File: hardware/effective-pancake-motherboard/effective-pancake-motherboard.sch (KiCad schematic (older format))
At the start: 45 parts, among them J1 Conn_02x05_Odd_Even, J2 Conn_02x04_Odd_Even, J5 QTR-1A_Conn, J6 QTR-1A_Conn, U1 Teensy_3.2, U3 Teensy_3.6, U4 SN74AHCT125N, U5 TMC2660-BOB, U6 TMC2660-BOB, U7 TMC2660-BOB

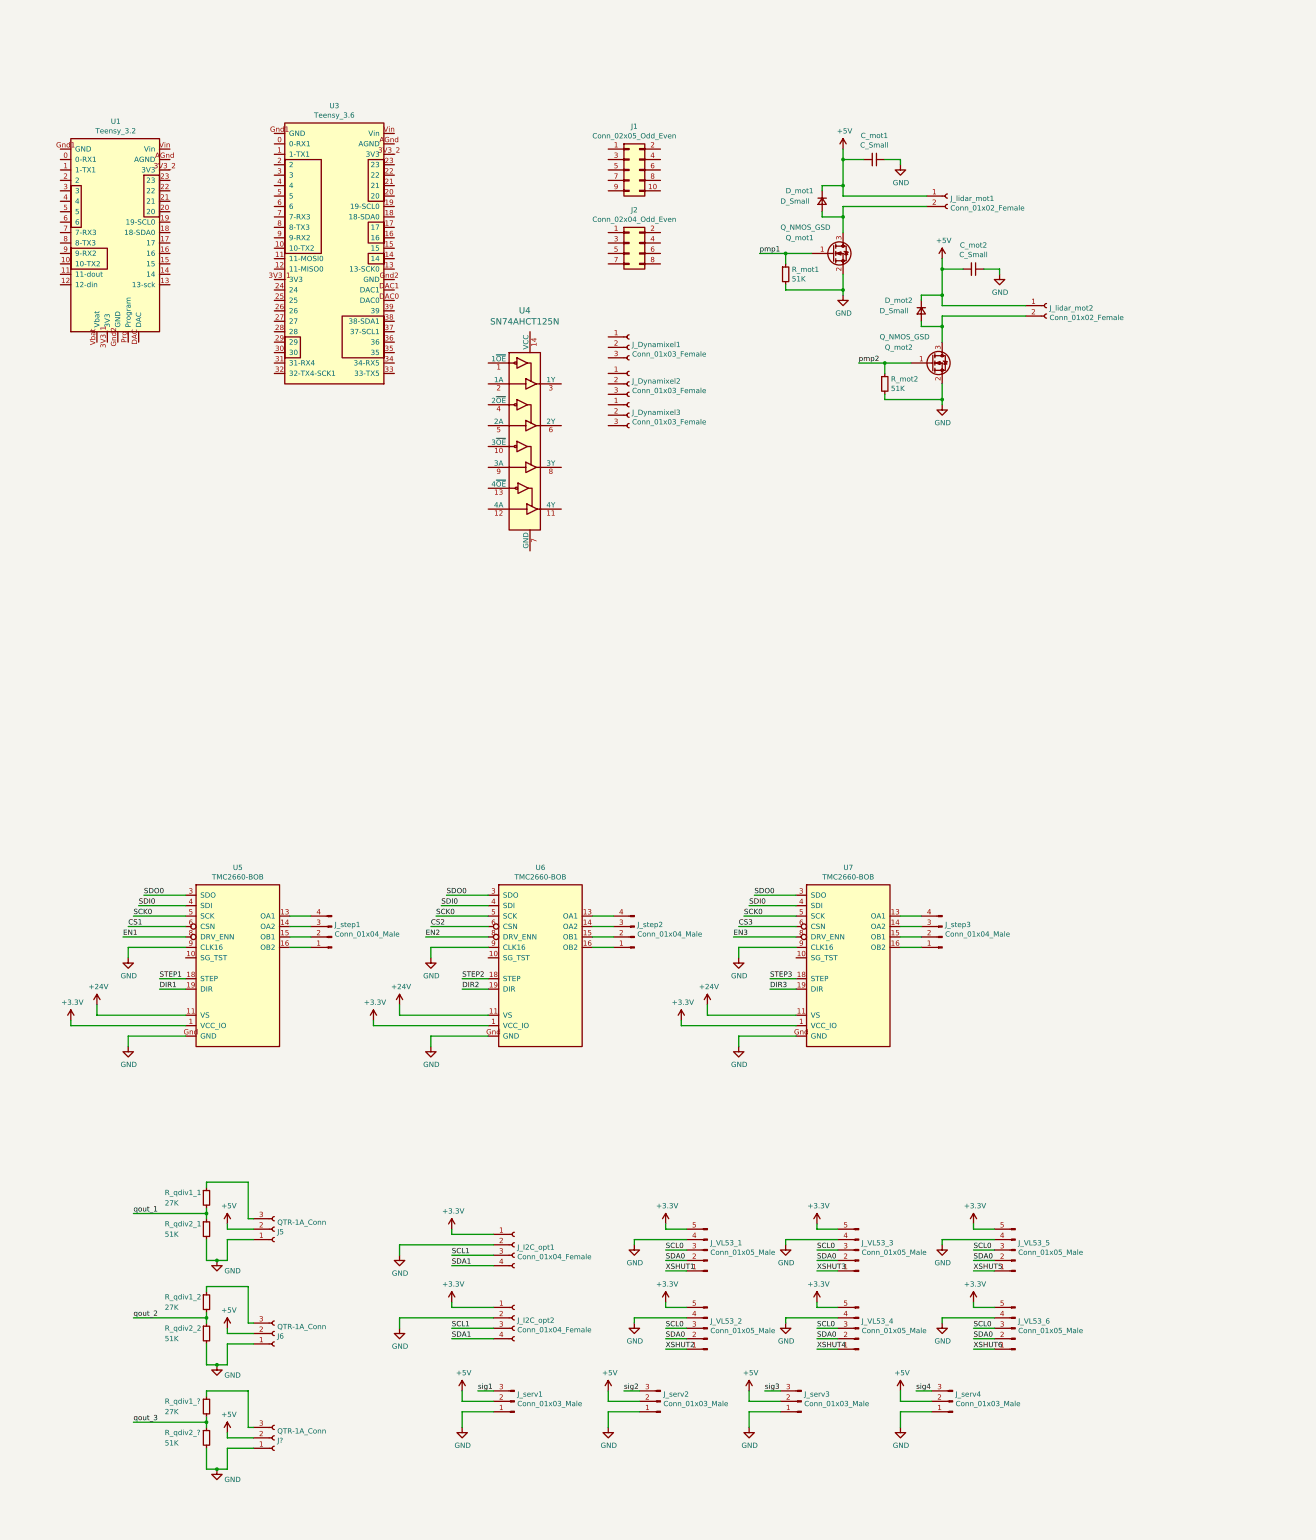
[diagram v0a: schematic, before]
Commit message: Finished schematics, fp association, and verifications.
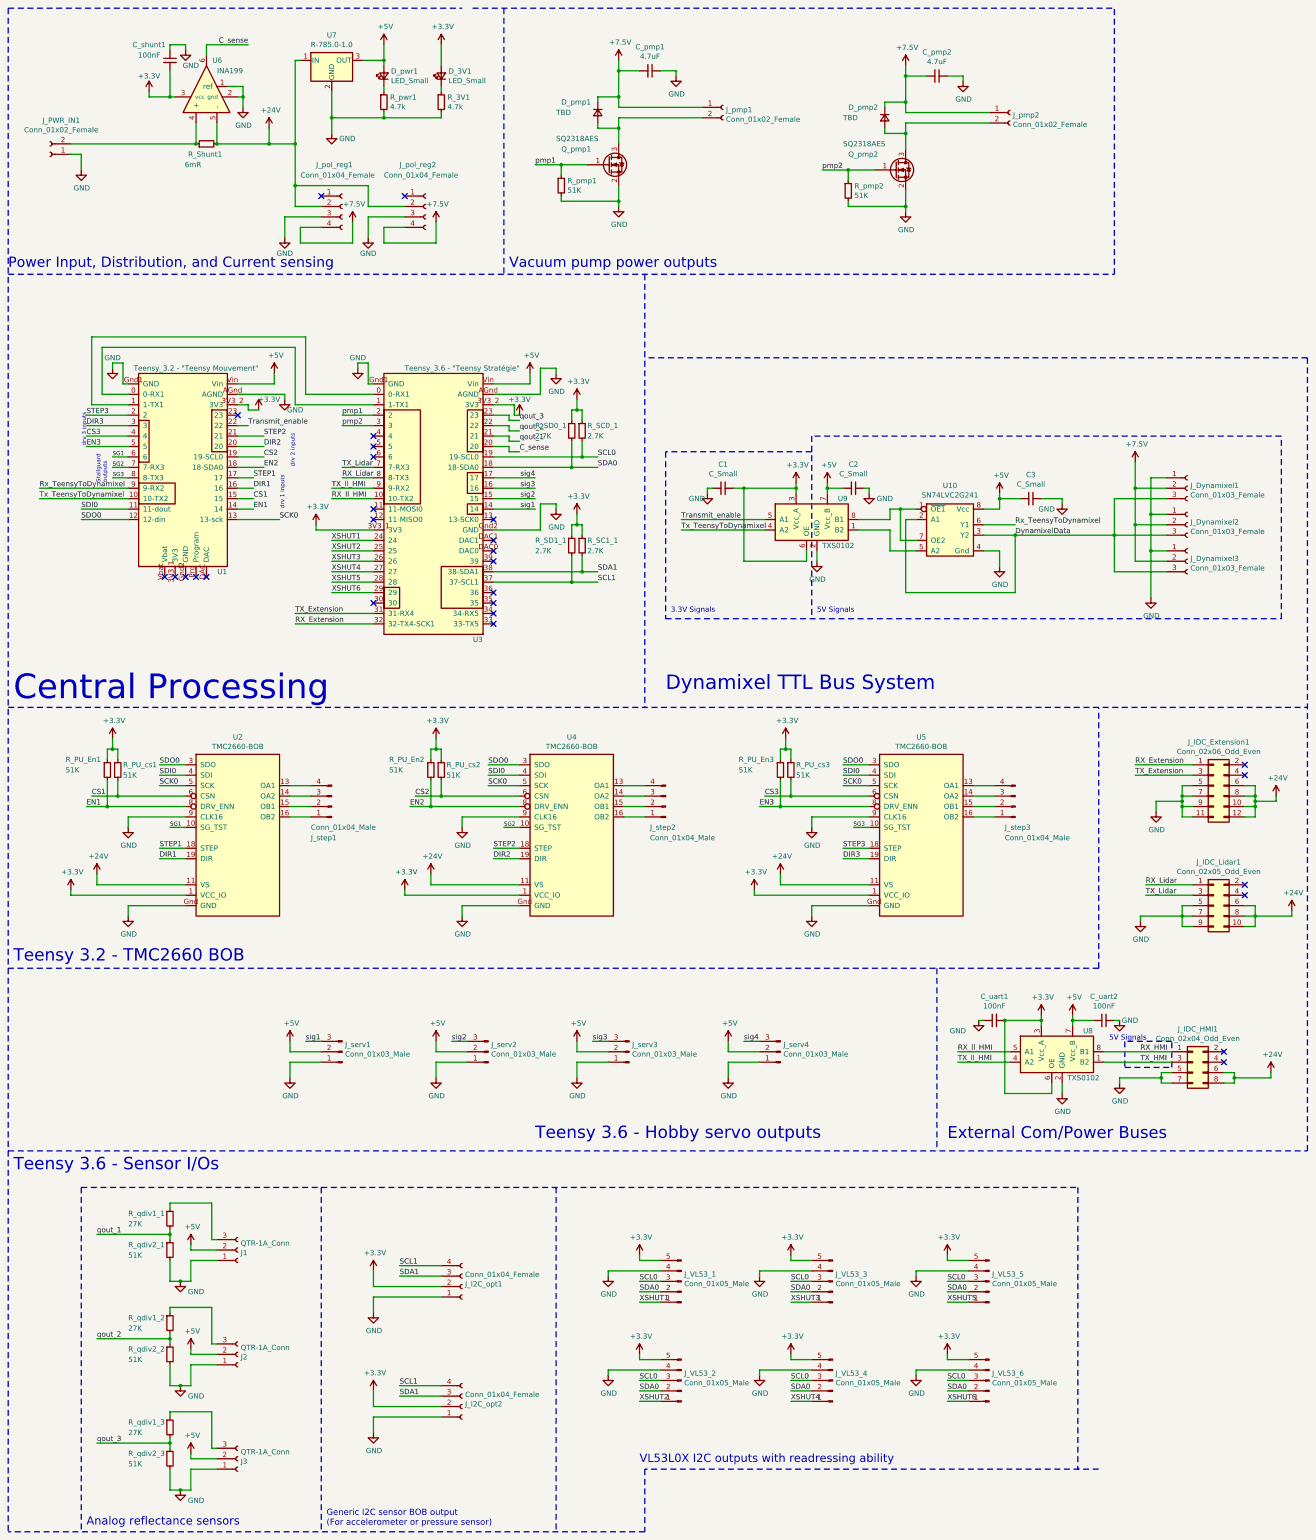
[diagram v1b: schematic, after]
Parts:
- removed U4: SN74AHCT125N, digikey-footprints:DIP-14_W3mm, symbol dk_Logic-Buffers-Drivers-Receivers-Transceivers:SN74AHCT125N
- added C1, C2, C3: C_Small, Capacitor_SMD:C_0805_2012Metric_Pad1.15x1.40mm_HandSolder, symbol Device:C_Small
- added C_shunt1, C_uart1, C_uart2: 100nF, Capacitor_SMD:C_0805_2012Metric_Pad1.15x1.40mm_HandSolder, symbol Device:C_Small
- added D_3V1, D_pwr1: LED_Small, LED_SMD:LED_1206_3216Metric_Castellated, symbol Device:LED_Small
- added J_IDC_Extension1: Conn_02x06_Odd_Even, Connector_IDC:IDC-Header_2x06_P2.54mm_Vertical, symbol Connector_Generic:Conn_02x06_Odd_Even
- added J_PWR_IN1: Conn_01x02_Female, Connector_Phoenix_MC_HighVoltage:PhoenixContact_MC_1,5_2-G-5.08_1x02_P5.08mm_Horizontal, symbol Connector:Conn_01x02_Female
- added J_pol_reg1, J_pol_reg2: Conn_01x04_Female, Connector_PinSocket_2.54mm:PinSocket_1x04_P2.54mm_Vertical, symbol Connector:Conn_01x04_Female
- added R_3V1, R_pwr1: 4.7k, Resistor_SMD:R_0805_2012Metric_Pad1.15x1.40mm_HandSolder, symbol Device:R_Small
- added R_PU_En1, R_PU_En2, R_PU_En3, R_PU_cs1, R_PU_cs2, R_PU_cs3: 51K, Resistor_SMD:R_0805_2012Metric_Pad1.15x1.40mm_HandSolder, symbol Device:R_Small
- added R_SC0_1, R_SC1_1, R_SD0_1, R_SD1_1: 2.7K, Resistor_SMD:R_0805_2012Metric_Pad1.15x1.40mm_HandSolder, symbol Device:R_Small
- added R_Shunt1: 6mR, Resistor_SMD:R_1206_3216Metric_Pad1.42x1.75mm_HandSolder, symbol Device:R_Small
- added U10: SN74LVC2G241, effective-pancake_fp:PDSO-G8, symbol effective-pancake-global:SN74LVC2G241
- added U6: INA199, Package_TO_SOT_SMD:Texas_R-PDSO-G6, symbol effective-pancake-global:INA199
- added U7: R-785.0-1.0, Converter_DCDC:Converter_DCDC_RECOM_R-78E-0.5_THT, symbol effective-pancake-global:R-785.0-1.0
- added U8, U9: TXS0102, effective-pancake_fp:PDSO-G8, symbol effective-pancake-global:TXS0102
- C_pmp1: renamed from C_mot1; value C_Small -> 4.7uF; footprint (none) -> Capacitor_THT:C_Radial_D4.0mm_H7.0mm_P1.50mm
- C_pmp2: renamed from C_mot2; value C_Small -> 4.7uF; footprint (none) -> Capacitor_THT:C_Radial_D4.0mm_H7.0mm_P1.50mm
- D_pmp1: renamed from D_mot1; value D_Small -> TBD; footprint (none) -> Diode_SMD:D_1206_3216Metric
- D_pmp2: renamed from D_mot2; value D_Small -> TBD; footprint (none) -> Diode_SMD:D_1206_3216Metric
- J_Dynamixel1, J_Dynamixel2, J_Dynamixel3: footprint (none) -> Connector_Molex:Molex_Micro-Latch_53253-0370_1x03_P2.00mm_Vertical
- J_I2C_opt1, J_I2C_opt2: footprint (none) -> Connector_PinSocket_2.54mm:PinSocket_1x04_P2.54mm_Vertical
- J_IDC_HMI1: renamed from J2; footprint (none) -> Connector_IDC:IDC-Header_2x04_P2.54mm_Vertical
- J_IDC_Lidar1: renamed from J1; footprint (none) -> Connector_IDC:IDC-Header_2x05_P2.54mm_Vertical
- J_VL53_1, J_VL53_2, J_VL53_3, J_VL53_4, J_VL53_5, J_VL53_6: footprint (none) -> Connector_PinSocket_2.54mm:PinSocket_1x05_P2.54mm_Vertical
- J_pmp1: renamed from J_lidar_mot1; footprint (none) -> Connector_JST:JST_XH_B2B-XH-A_1x02_P2.50mm_Vertical
- J_pmp2: renamed from J_lidar_mot2; footprint (none) -> Connector_JST:JST_XH_B2B-XH-A_1x02_P2.50mm_Vertical
- J_serv1, J_serv2, J_serv3, J_serv4: footprint (none) -> Connector_PinHeader_2.54mm:PinHeader_1x03_P2.54mm_Vertical
- J_step1, J_step2, J_step3: footprint (none) -> Connector_PinHeader_2.54mm:PinHeader_1x04_P2.54mm_Vertical
- Q_pmp1: renamed from Q_mot1; value Q_NMOS_GSD -> SQ2318AES; footprint (none) -> Package_TO_SOT_SMD:SOT-23
- Q_pmp2: renamed from Q_mot2; value Q_NMOS_GSD -> SQ2318AES; footprint (none) -> Package_TO_SOT_SMD:SOT-23
- R_pmp1: renamed from R_mot1; footprint (none) -> Resistor_SMD:R_0805_2012Metric_Pad1.15x1.40mm_HandSolder
- R_pmp2: renamed from R_mot2; footprint (none) -> Resistor_SMD:R_0805_2012Metric_Pad1.15x1.40mm_HandSolder
- U1: value Teensy_3.2 -> Teensy_3.2 - \"Teensy Mouvement\"; footprint (none) -> digikey-footprints:Teensy_3.2
- U2: renamed from U5; footprint (none) -> effective-pancake_fp:TMC2660-BOB
- U3: value Teensy_3.6 -> Teensy_3.6 - \"Teensy Stratégie\"; footprint (none) -> effective-pancake_fp:Teensy_3.6
- U4: renamed from U6; footprint (none) -> effective-pancake_fp:TMC2660-BOB
- U5: renamed from U7; footprint (none) -> effective-pancake_fp:TMC2660-BOB
- gave numbers to parts that had none: 3
- renumbered J5 to J1, J6 to J2
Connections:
- net +24V: now also J_IDC_HMI1.6 (Pin_6), J_IDC_HMI1.8 (Pin_8), J_IDC_Lidar1.10 (Pin_10), J_IDC_Lidar1.6 (Pin_6), J_IDC_Lidar1.8 (Pin_8), J_IDC_Extension1.10 (Pin_10), J_IDC_Extension1.12 (Pin_12), J_IDC_Extension1.6 (Pin_6), J_IDC_Extension1.8 (Pin_8), J_pol_reg1.2 (Pin_2), J_pol_reg2.2 (Pin_2), R_Shunt1.2, U6.5 (-), U7.1 (IN)
- net +3V3: now also J_I2C_opt1.2 (Pin_2), J_I2C_opt2.2 (Pin_2), U1.3V3_2 (3V3), U3.3V3_1 (3V3), U3.3V3_2 (3V3), C1.1, C_shunt1.2, C_uart1.2, D_3V1.2 (A), R_PU_En1.1, R_PU_En2.1, R_PU_En3.1, R_PU_cs1.1, R_PU_cs2.1, R_PU_cs3.1, R_SC0_1.1, R_SC1_1.1, R_SD0_1.1, R_SD1_1.1, U6.3 (vcc), U8.3 (Vcc_A), U8.6 (OE), U9.3 (Vcc_A), U9.6 (OE); no longer J_I2C_opt1.1 (Pin_1), J_I2C_opt2.1 (Pin_1)
- net +5V: now also U1.Vin, U3.Vin, C2.2, C3.2, C_uart2.2, D_pwr1.2 (A), U10.8 (Vcc), U7.3 (OUT), U8.7 (Vcc_B), U9.7 (Vcc_B); no longer C_pmp1.2, C_pmp2.2, D_pmp1.1 (K), D_pmp2.1 (K), J_pmp1.1 (Pin_1), J_pmp2.1 (Pin_1)
- net CS1: now also U1.15, R_PU_cs1.2
- net CS2: now also U1.19 (19-SCL0), R_PU_cs2.2
- net CS3: now also U1.4, R_PU_cs3.2
- net DIR1: now also U1.16
- net DIR2: now also U1.20
- net DIR3: now also U1.3
- net EN1: now also U1.14, R_PU_En1.2
- net EN2: now also U1.18 (18-SDA0), R_PU_En2.2
- net EN3: now also U1.5, R_PU_En3.2
- net GND: now also J_Dynamixel1.1 (Pin_1), J_Dynamixel2.1 (Pin_1), J_Dynamixel3.1 (Pin_1), J_I2C_opt1.1 (Pin_1), J_I2C_opt2.1 (Pin_1), J_IDC_HMI1.5 (Pin_5), J_IDC_HMI1.7 (Pin_7), J_IDC_Lidar1.5 (Pin_5), J_IDC_Lidar1.7 (Pin_7), J_IDC_Lidar1.9 (Pin_9), U1.AGnd (AGND), U1.Gnd1 (GND), U3.AGnd (AGND), U3.Gnd1 (GND), U3.Gnd2 (GND), C1.2, C2.1, C3.1, C_shunt1.1, C_uart1.1, C_uart2.1, J_IDC_Extension1.11 (Pin_11), J_IDC_Extension1.5 (Pin_5), J_IDC_Extension1.7 (Pin_7), J_IDC_Extension1.9 (Pin_9), J_PWR_IN1.1 (Pin_1), J_pol_reg1.3 (Pin_3), J_pol_reg2.3 (Pin_3), R_3V1.2, R_pwr1.2, U10.4 (Gnd), U6.1 (ref), U6.2 (gnd), U7.2 (GND), U8.2 (GND), U9.2 (GND); no longer J_I2C_opt1.2 (Pin_2), J_I2C_opt2.2 (Pin_2)
- net SCK0: now also U1.13 (13-sck)
- net SCL0: now also U3.19 (19-SCL0), R_SC0_1.2
- net SCL1: now also J_I2C_opt1.4 (Pin_4), J_I2C_opt2.4 (Pin_4), U3.37 (37-SCL1), R_SD1_1.2; no longer J_I2C_opt1.3 (Pin_3), J_I2C_opt2.3 (Pin_3)
- net SDA0: now also U3.18 (18-SDA0), R_SD0_1.2
- net SDA1: now also J_I2C_opt1.3 (Pin_3), J_I2C_opt2.3 (Pin_3), U3.38 (38-SDA1), R_SC1_1.2; no longer J_I2C_opt1.4 (Pin_4), J_I2C_opt2.4 (Pin_4)
- net SDI0: now also U1.11 (11-dout)
- net SDO0: now also U1.12 (12-din)
- net STEP1: now also U1.17
- net STEP2: now also U1.21
- net STEP3: now also U1.2
- net XSHUT1: now also U3.24
- net XSHUT2: now also U3.25
- net XSHUT3: now also U3.26
- net XSHUT4: now also U3.27
- net XSHUT5: now also U3.28
- net XSHUT6: now also U3.29
- net pmp1: now also U3.2
- net pmp2: now also U3.3
- net qout_1: now also U3.21
- net qout_2: now also U3.22
- net qout_3: now also U3.23
- net sig1: now also U3.14
- net sig2: now also U3.15
- net sig3: now also U3.16
- net sig4: now also U3.17
- net at U1.0 (0-RX1): now also U3.1 (1-TX1)
- net at U1.1 (1-TX1): now also U3.0 (0-RX1)
- net Tx_TeensyToDynamixel: now reaches U1.10 (10-TX2)
- net Tx_TeensyToDynamixel: now also U9.4 (A2)
- net Transmit_enable: now reaches U1.22
- net Transmit_enable: now also U9.5 (A1)
- net SG1: now reaches U1.6
- net SG1: now also U2.10 (SG_TST)
- net SG2: now reaches U1.7 (7-RX3)
- net SG2: now also U4.10 (SG_TST)
- net SG3: now reaches U1.8 (8-TX3)
- net SG3: now also U5.10 (SG_TST)
- net Rx_TeensyToDynamixel: now reaches U1.9 (9-RX2)
- net Rx_TeensyToDynamixel: now also U10.6 (Y1)
- net RX_ll_HMI: now reaches U3.10 (10-TX2)
- net RX_ll_HMI: now also U8.5 (A1)
- net C_sense: now reaches U3.20
- net C_sense: now also U6.6
- net TX_Extension: now reaches U3.31 (31-RX4)
- net TX_Extension: now also J_IDC_Extension1.3 (Pin_3)
- net RX_Extension: now reaches U3.32 (32-TX4-SCK1)
- net RX_Extension: now also J_IDC_Extension1.1 (Pin_1)
- net TX_Lidar: now reaches U3.7 (7-RX3)
- net TX_Lidar: now also J_IDC_Lidar1.3 (Pin_3)
- net RX_Lidar: now reaches U3.8 (8-TX3)
- net RX_Lidar: now also J_IDC_Lidar1.1 (Pin_1)
- net TX_ll_HMI: now reaches U3.9 (9-RX2)
- net TX_ll_HMI: now also U8.4 (A2)
- net RX_HMI: now reaches J_IDC_HMI1.1 (Pin_1)
- net RX_HMI: now also U8.8 (B1)
- net TX_HMI: now reaches J_IDC_HMI1.3 (Pin_3)
- net TX_HMI: now also U8.1 (B2)
- net +7.5V: now reaches J_Dynamixel1.2 (Pin_2)
- net +7.5V: now also C_pmp1.2, C_pmp2.2, D_pmp1.1 (K), D_pmp2.1 (K), J_Dynamixel2.2 (Pin_2), J_Dynamixel3.2 (Pin_2), J_pmp1.1 (Pin_1), J_pmp2.1 (Pin_1), J_pol_reg1.4 (Pin_4), J_pol_reg2.4 (Pin_4)
- net DynamixelData: now reaches J_Dynamixel1.3 (Pin_3)
- net DynamixelData: now also J_Dynamixel2.3 (Pin_3), J_Dynamixel3.3 (Pin_3), U10.2 (A1), U10.3 (Y2)
- new net: U10.1 (~OE1), U10.7 (OE2), U9.8 (B1)
- new net: U10.5 (A2), U9.1 (B2)
- new net: J_PWR_IN1.2 (Pin_2), R_Shunt1.1, U6.4 (+)
- new net: D_pwr1.1 (K), R_pwr1.1
- new net: D_3V1.1 (K), R_3V1.1
- no-connect marks 0 -> 28
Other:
- note added: "3.3V Signals\n"
- note added: "5V Signals\n"
- note added: "Analog reflectance sensors\n"
- note added: "Central Processing"
- note added: "Dynamixel TTL Bus System\n"
- note added: "External Com/Power Buses"
- note added: "Generic I2C sensor BOB output\n(For accelerometer or pressure sensor)\n"
- note added: "Power Input, Distribution, and Current sensing\n"
- note added: "Stallguard\noutputs\n"
- note added: "Teensy 3.2 - TMC2660 BOB \n"
- note added: "Teensy 3.6 - Hobby servo outputs\n"
- note added: "Teensy 3.6 - Sensor I/Os\n"
- note added: "VL53L0X I2C outputs with readressing ability\n"
- note added: "Vacuum pump power outputs"
- note added: "drv 1 inputs\n"
- note added: "drv 2 inputs\n"
- note added: "drv 3 inputs\n"
- moved on the sheet: C_pmp1, C_pmp2, D_pmp1, D_pmp2, J1, J2, J3, J_Dynamixel1, J_Dynamixel2, J_Dynamixel3, J_I2C_opt1, J_IDC_HMI1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
